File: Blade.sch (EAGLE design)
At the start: 100 parts, among them IC1 THN10-2411WIR, IC2 MCP6064-E/SL, IC3 MCP6064-E/SL, IC4 MCP6064-E/SL, Q1 12MHz, U1 ADR366WAUJZ, U2 ADR366WAUJZ, U3 ADS1148QPWRQ1, U4 ADS1148QPWRQ1, U5 ADS1148QPWRQ1, U6 LT1528, U7 S70FL01GS, U8 S70FL01GS, U9 STM32F77XXXLQFP208, X1 D-SUB9-H5M09RA, X2 D-SUB15-H5M15RA, X3 USBPTH

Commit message: opto added
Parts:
- added D5, D6, D7, D8, D9: 3V6, diodes:DZMELF
- added IC5: MAX488CSA, maxim:MAX488CSA
- added IC6, IC7: MOCD207MSOIC-8, Opto-Electronic:MOCD207MSOIC-8
- added R10: 1k, rcl:R-EU_R0805
- added RN11, RN12: 56k, resistor-dil:4R-NEXBS8V
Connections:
- new net EXP_IN: D5.C, IC5G$1.RO, U9.PE0
- new net EXP_OUT: D6.C, IC5G$1.DI, U9.PE1
- new net LO_OPT: D7.C, IC7.COL1, RN12C.2, U9.PI7
- new net N$42: IC6.A1, RN11C.2
- new net N$43: IC6.A2, RN11D.2
- new net N$45: IC7.COL2, RN12D.2
- new net N$46: IC7.A1, RN11A.2
- new net N$47: IC7.A2, RN11B.2
- new net N$48: IC7.C2
- new net SODS_OPT: D8.C, IC6.COL1, RN12A.2, U9.PI5
- new net SOE_OPT: D9.C, IC6.COL2, RN12B.2, U9.PI6
- net 28V: now also RN11A.1, RN11B.1, RN11C.1, RN11D.1
- net 3V3: now also IC5P.VCC, RN12A.1, RN12B.1, RN12C.1, RN12D.1
- net EXP_IN_N: now also IC5G$1.B, R10.1
- net EXP_IN_P: now also IC5G$1.A, R10.2
- net EXP_OUT_N: now also IC5G$1.Z
- net EXP_OUT_P: now also IC5G$1.Y
- net GND: now also D5.A, D6.A, D7.A, D8.A, D9.A, IC5P.GND, IC6.EMT1, IC6.EMT2, IC7.EMT1, IC7.EMT2
- net LO: now also IC7.C1
- net SODS: now also IC6.C1
- net SOE: now also IC6.C2

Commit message: cleanup
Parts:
- RN11: value 56k -> 3k
- RN12: value 56k -> 1k
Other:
- note added: "galv trenn?"
- moved on the sheet: C1, C10, C11, C12, C13, C14, C15, C19, C2, C20, C21, C22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

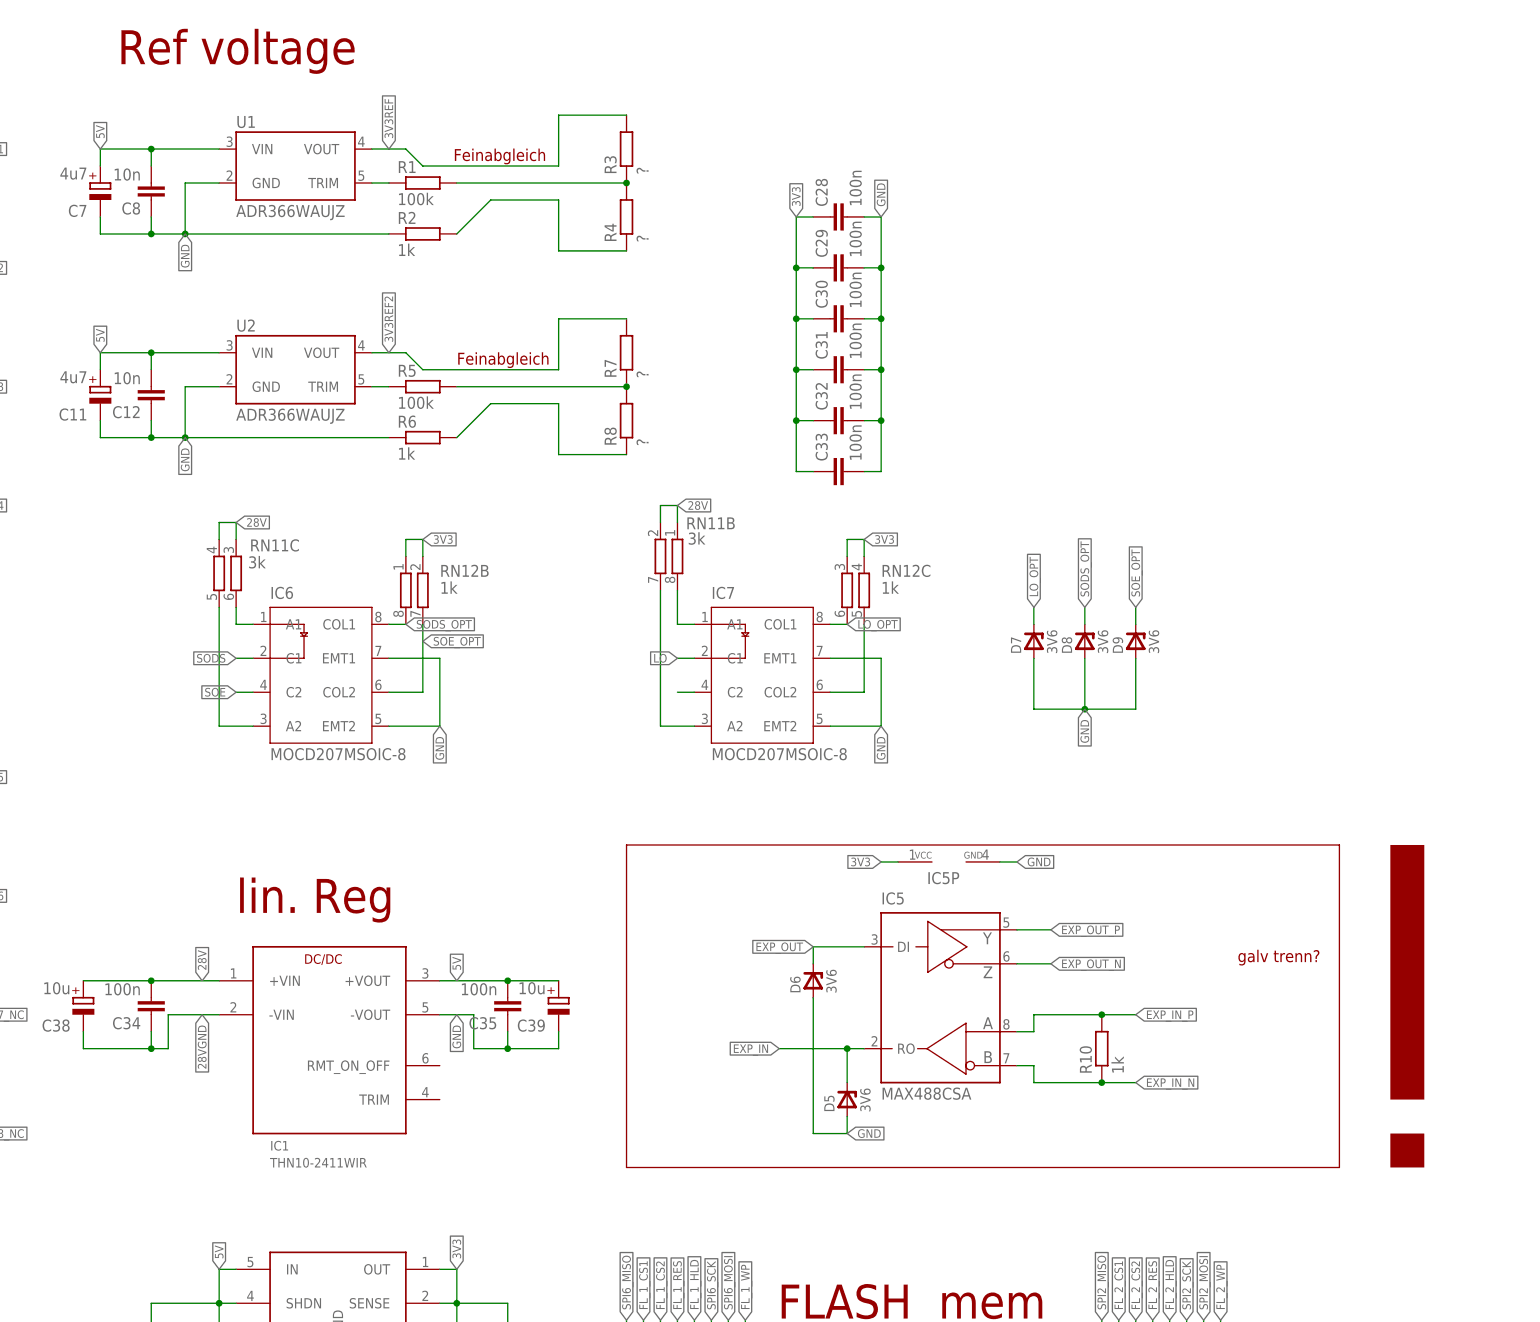
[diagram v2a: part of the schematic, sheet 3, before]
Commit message: RS422 opto galv isolation added
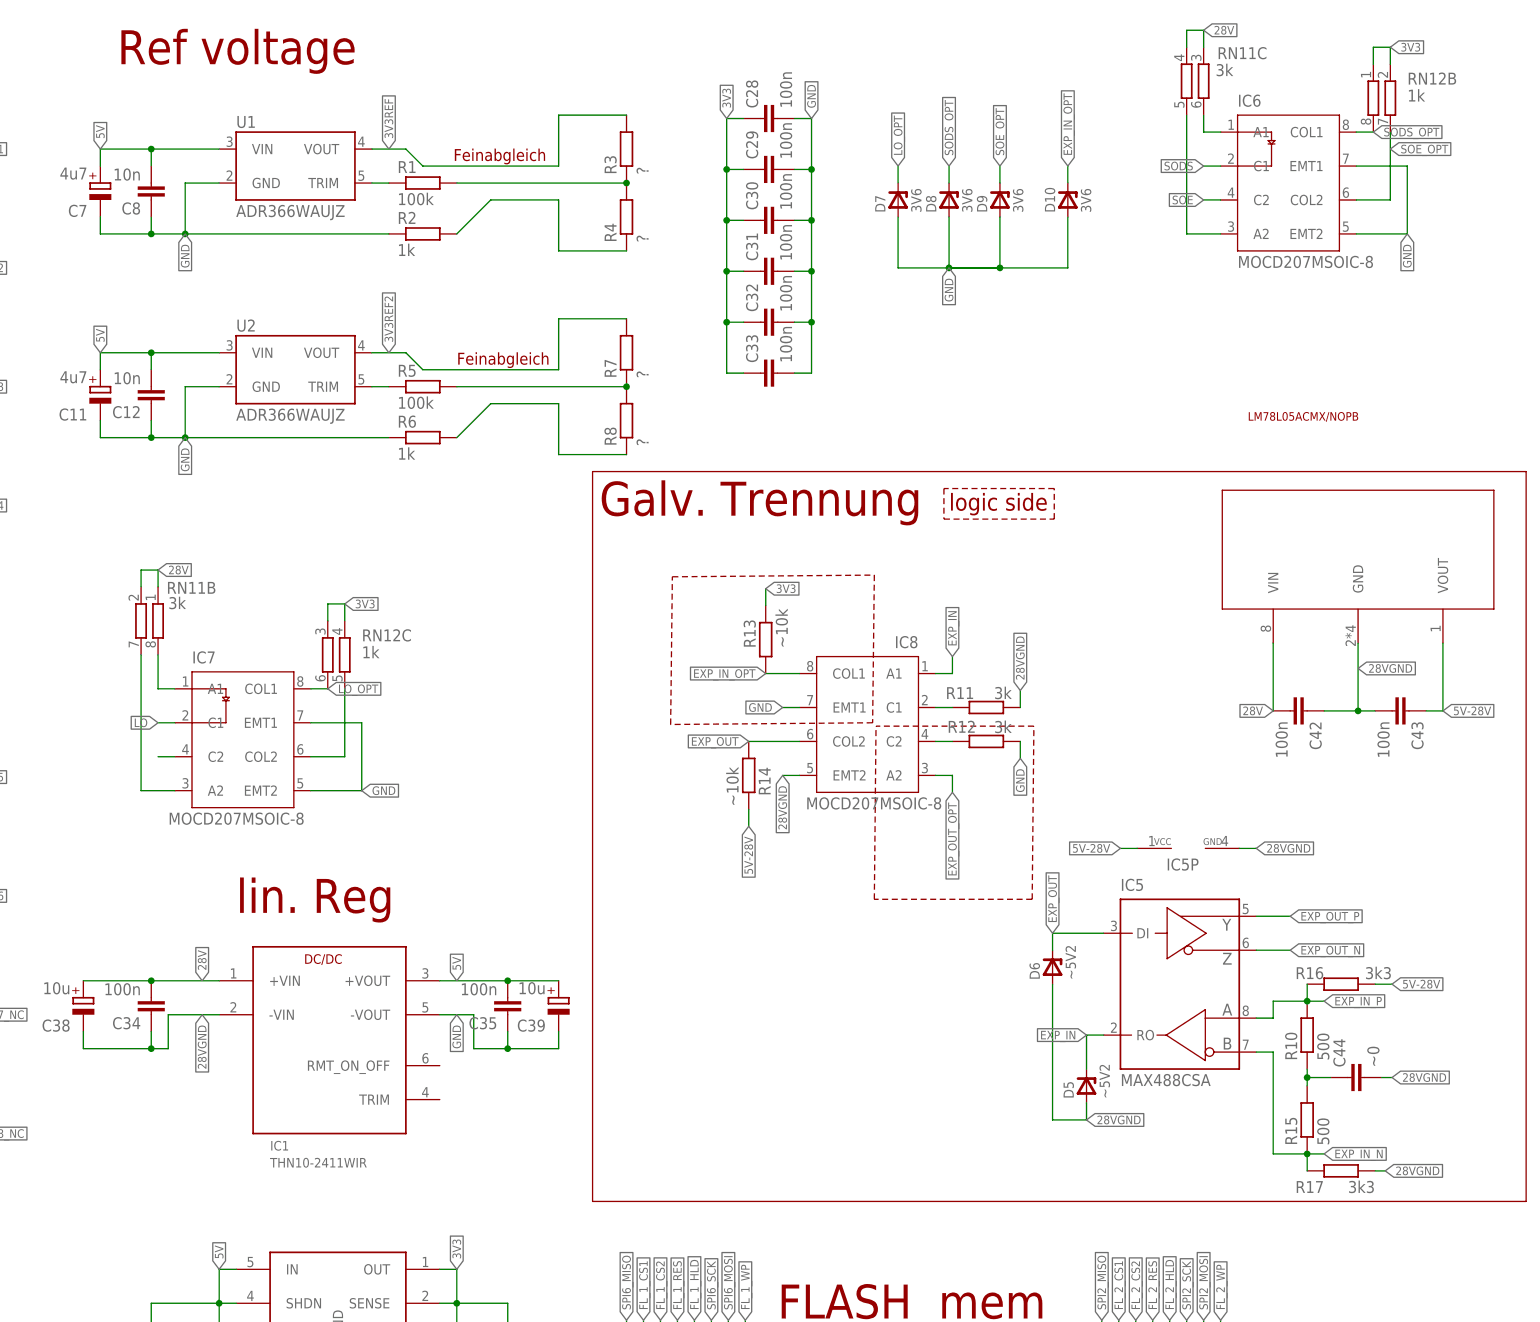
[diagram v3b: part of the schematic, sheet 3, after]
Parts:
- added C42, C43: 100n, rcl:C-EUC0805
- added C44: ~0, rcl:C-EUC0805
- added D10: 3V6, diodes:DZMELF
- added IC8: MOCD207MSOIC-8, Opto-Electronic:MOCD207MSOIC-8
- added R11, R12: 3k, rcl:R-EU_R0805
- added R13, R14: ~10k, rcl:R-EU_R0805
- added R15: 500, rcl:R-EU_R0805
- added R16, R17: 3k3, rcl:R-EU_R0805
- added U$1: LM78L05ACMX/NOPB, m-pad-2.1:LM78L05ACMX/NOPB
- D5, D6: value 3V6 -> ~5V2
- R10: value 1k -> 500
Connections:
- new net 5V-28V: C43.1, IC5P.VCC, R14.2, R16.1, U$1.VOUT
- new net EXP_IN_OPT: D10.C, IC8.COL1, R13.1
- new net EXP_OUT_OPT: IC8.A2
- new net N$44: IC8.C2, R12.2
- new net N$49: IC8.C1, R11.2
- new net N$50: C44.1, R10.1, R15.2
- net 28V: now also C42.2, U$1.VIN
- net 28VGND: now also C42.1, C43.2, C44.2, D5.A, D6.A, IC5P.GND, IC8.EMT2, R11.1, R17.1, U$1.GND
- net 3V3: now also R13.2; no longer IC5P.VCC
- net EXP_IN: now also IC8.A1
- net EXP_IN_N: now also R15.1, R17.2; no longer R10.1
- net EXP_IN_P: now also R16.2
- net EXP_OUT: now also IC8.COL2, R14.1
- net GND: now also D10.A, IC8.EMT1, R12.1; no longer D5.A, D6.A, IC5P.GND
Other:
- note added: "Galv. Trennung"
- note added: "LM78L05ACMX/NOPB"
- note added: "logic side"
- note removed: "galv trenn?"
- moved on the sheet: C28, C29, C30, C31, C32, C33, D5, D6, D7, D8, D9, IC5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

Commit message: rerouting
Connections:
- net 28V: no longer X1-8.F
- net 28VGND: now also X1-8.F
- net EXP_IN: no longer U9.PE0
- net EXP_IN_OPT: now also U9.PE0
- net EXP_OUT: no longer U9.PE1
- net EXP_OUT_OPT: now also U9.PE1
- net LED_1: now also U9.PF5
- net LED_2: now also U9.PF4
- net LED_3: now also U9.PF3
- net LED_4: now also U9.PI14
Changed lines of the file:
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@@
 </segment>
 </net>
-<net name="EXP_IN" class="0">
+<net name="EXP_OUT_OPT" class="0">
+<segment>
+<pinref part="U9" gate="G$1" pin="PE1"/>
+<wire x1="383.54" y1="142.24" x2="383.54" y2="137.16" width="0.1524" layer="91"/>
+<label x="383.54" y="137.16" size="1.27" layer="95" rot="R270" xref="yes"/>
+</segment>
+</net>
+<net name="EXP_IN_OPT" class="0">
 <segment>
 <pinref part="U9" gate="G$1" pin="PE0"/>
@@
 </segment>
 </net>
-<net name="EXP_OUT" class="0">
-<segment>
-<pinref part="U9" gate="G$1" pin="PE1"/>
-<wire x1="383.54" y1="142.24" x2="383.54" y2="137.16" width="0.1524" layer="91"/>
-<label x="383.54" y="137.16" size="1.27" layer="95" rot="R270" xref="yes"/>
+<net name="LED_1" class="0">
+<segment>
+<pinref part="U9" gate="G$1" pin="PF5"/>
+<wire x1="276.86" y1="142.24" x2="276.86" y2="137.16" width="0.1524" layer="91"/>
+<label x="276.86" y="137.16" size="1.27" layer="95" rot="R270" xref="yes"/>
+</segment>
+</net>
+<net name="LED_2" class="0">
+<segment>
+<pinref part="U9" gate="G$1" pin="PF4"/>
+<wire x1="281.94" y1="142.24" x2="281.94" y2="137.16" width="0.1524" layer="91"/>
+<label x="281.94" y="137.16" size="1.27" layer="95" rot="R270" xref="yes"/>
+</segment>
+</net>
+<net name="LED_3" class="0">
+<segment>
+<pinref part="U9" gate="G$1" pin="PF3"/>
+<wire x1="287.02" y1="142.24" x2="287.02" y2="137.16" width="0.1524" layer="91"/>
+<label x="287.02" y="137.16" size="1.27" layer="95" rot="R270" xref="yes"/>
+</segment>
+</net>
+<net name="LED_4" class="0">
+<segment>
+<pinref part="U9" gate="G$1" pin="PI14"/>
+<wire x1="210.82" y1="401.32" x2="205.74" y2="401.32" width="0.1524" layer="91"/>
+<label x="205.74" y="401.32" size="1.27" layer="95" rot="R180" xref="yes"/>
 </segment>
 </net>
@@
 </segment>
 <segment>
-<pinref part="X1" gate="-8" pin="F"/>
-<wire x1="104.14" y1="124.46" x2="109.22" y2="124.46" width="0.1524" layer="91"/>
-<wire x1="109.22" y1="124.46" x2="109.22" y2="127" width="0.1524" layer="91"/>
 <pinref part="X1" gate="-9" pin="F"/>
 <wire x1="109.22" y1="127" x2="104.14" y2="127" width="0.1524" layer="91"/>
@@
 <label x="106.68" y="172.72" size="1.27" layer="95" xref="yes"/>
 <pinref part="X2" gate="-15" pin="F"/>
+</segment>
+<segment>
+<pinref part="X1" gate="-8" pin="F"/>
+<wire x1="104.14" y1="124.46" x2="109.22" y2="124.46" width="0.1524" layer="91"/>
+<label x="109.22" y="124.46" size="1.27" layer="95" xref="yes"/>
 </segment>
 </net>
@@
 <wire x1="442.468" y1="226.06" x2="425.958" y2="226.06" width="0.1524" layer="94" style="shortdash"/>
 <wire x1="425.958" y1="226.06" x2="425.958" y2="221.488" width="0.1524" layer="94" style="shortdash"/>
+<wire x1="477.52" y1="256.54" x2="477.52" y2="297.18" width="0.1524" layer="94" style="shortdash"/>
+<wire x1="477.52" y1="297.18" x2="513.08" y2="297.18" width="0.1524" layer="94" style="shortdash"/>
+<wire x1="513.08" y1="297.18" x2="513.08" y2="256.54" width="0.1524" layer="94" style="shortdash"/>
+<wire x1="513.08" y1="256.54" x2="477.52" y2="256.54" width="0.1524" layer="94" style="shortdash"/>
 </plain>
 <instances>

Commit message: ground vias
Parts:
- added LED5, LED6, LED7, LED8: (no value), adafruit:LEDCHIP-LED0603
- added R18, R19, R20, R21: ?, rcl:R-EU_R0805
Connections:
- new net N$51: LED5.A, R18.1
- new net N$52: LED6.A, R19.1
- new net N$55: LED7.A, R20.1
- new net N$56: LED8.A, R21.1
- net 28V: now also R20.2
- net 28VGND: now also LED7.C, LED8.C
- net 3V3: now also R19.2
- net 5V: now also R18.2
- net 5V-28V: now also R21.2
- net GND: now also LED5.C, LED6.C
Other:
- note added: "V. Reg"
- note removed: "lin. Reg"
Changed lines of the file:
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@@
 <part name="R16" library="rcl" deviceset="R-EU_" device="R0805" value="3k3"/>
 <part name="R17" library="rcl" deviceset="R-EU_" device="R0805" value="3k3"/>
+<part name="LED5" library="adafruit" library_urn="urn:adsk.eagle:library:420" deviceset="LED" device="CHIP-LED0603" package3d_urn="urn:adsk.eagle:package:6240556/1"/>
+<part name="LED6" library="adafruit" library_urn="urn:adsk.eagle:library:420" deviceset="LED" device="CHIP-LED0603" package3d_urn="urn:adsk.eagle:package:6240556/1"/>
+<part name="R18" library="rcl" library_urn="urn:adsk.eagle:library:334" deviceset="R-EU_" device="R0805" package3d_urn="urn:adsk.eagle:package:23553/2" value="?"/>
+<part name="R19" library="rcl" library_urn="urn:adsk.eagle:library:334" deviceset="R-EU_" device="R0805" package3d_urn="urn:adsk.eagle:package:23553/2" value="?"/>
+<part name="LED7" library="adafruit" library_urn="urn:adsk.eagle:library:420" deviceset="LED" device="CHIP-LED0603" package3d_urn="urn:adsk.eagle:package:6240556/1"/>
+<part name="R20" library="rcl" library_urn="urn:adsk.eagle:library:334" deviceset="R-EU_" device="R0805" package3d_urn="urn:adsk.eagle:package:23553/2" value="?"/>
+<part name="LED8" library="adafruit" library_urn="urn:adsk.eagle:library:420" deviceset="LED" device="CHIP-LED0603" package3d_urn="urn:adsk.eagle:package:6240556/1"/>
+<part name="R21" library="rcl" library_urn="urn:adsk.eagle:library:334" deviceset="R-EU_" device="R0805" package3d_urn="urn:adsk.eagle:package:23553/2" value="?"/>
 </parts>
 <sheets>
@@
   UART</text>
 <text x="401.066" y="101.854" size="5.08" layer="94">FLASH  mem</text>
-<text x="320.04" y="162.56" size="5.08" layer="94">lin. Reg</text>
+<text x="320.04" y="162.56" size="5.08" layer="94">V. Reg</text>
 <wire x1="469.9" y1="279.4" x2="474.98" y2="279.4" width="0.1524" layer="94"/>
 <wire x1="474.98" y1="279.4" x2="474.98" y2="278.13" width="0.1524" layer="94"/>
@@
 <attribute name="NAME" x="25.4" y="73.152" size="1.778" layer="95"/>
 </instance>
+<instance part="LED5" gate="G$1" x="43.18" y="83.82" smashed="yes" rot="R90">
+<attribute name="NAME" x="47.752" y="87.376" size="1.778" layer="95" rot="R180"/>
+<attribute name="VALUE" x="47.752" y="89.535" size="1.778" layer="96" rot="R180"/>
+</instance>
+<instance part="LED6" gate="G$1" x="43.18" y="91.44" smashed="yes" rot="R90">
+<attribute name="NAME" x="47.752" y="94.996" size="1.778" layer="95" rot="R180"/>
+<attribute name="VALUE" x="47.752" y="97.155" size="1.778" layer="96" rot="R180"/>
+</instance>
+<instance part="R18" gate="G$1" x="33.02" y="83.82" smashed="yes" rot="R180">
+<attribute name="NAME" x="36.83" y="82.3214" size="1.778" layer="95" rot="R180"/>
+<attribute name="VALUE" x="36.83" y="87.122" size="1.778" layer="96" rot="R180"/>
+</instance>
+<instance part="R19" gate="G$1" x="33.02" y="91.44" smashed="yes" rot="R180">
+<attribute name="NAME" x="36.83" y="89.9414" size="1.778" layer="95" rot="R180"/>
+<attribute name="VALUE" x="36.83" y="94.742" size="1.778" layer="96" rot="R180"/>
+</instance>
+<instance part="LED7" gate="G$1" x="43.18" y="99.06" smashed="yes" rot="R90">
+<attribute name="NAME" x="47.752" y="102.616" size="1.778" layer="95" rot="R180"/>
+<attribute name="VALUE" x="47.752" y="104.775" size="1.778" layer="96" rot="R180"/>
+</instance>
+<instance part="R20" gate="G$1" x="33.02" y="99.06" smashed="yes" rot="R180">
+<attribute name="NAME" x="36.83" y="97.5614" size="1.778" layer="95" rot="R180"/>
+<attribute name="VALUE" x="36.83" y="102.362" size="1.778" layer="96" rot="R180"/>
+</instance>
+<instance part="LED8" gate="G$1" x="43.18" y="106.68" smashed="yes" rot="R90">
+<attribute name="NAME" x="47.752" y="110.236" size="1.778" layer="95" rot="R180"/>
+<attribute name="VALUE" x="47.752" y="112.395" size="1.778" layer="96" rot="R180"/>
+</instance>
+<instance part="R21" gate="G$1" x="33.02" y="106.68" smashed="yes" rot="R180">
+<attribute name="NAME" x="36.83" y="105.1814" size="1.778" layer="95" rot="R180"/>
+<attribute name="VALUE" x="36.83" y="109.982" size="1.778" layer="96" rot="R180"/>
+</instance>
 </instances>
 <busses>
@@
 <junction x="50.8" y="60.96"/>
 <label x="50.8" y="53.34" size="1.27" layer="95" xref="yes"/>
+<wire x1="50.8" y1="76.2" x2="50.8" y2="83.82" width="0.1524" layer="91"/>
+<junction x="50.8" y="76.2"/>
+<pinref part="LED6" gate="G$1" pin="C"/>
+<wire x1="50.8" y1="83.82" x2="50.8" y2="91.44" width="0.1524" layer="91"/>
+<wire x1="50.8" y1="91.44" x2="48.26" y2="91.44" width="0.1524" layer="91"/>
+<pinref part="LED5" gate="G$1" pin="C"/>
+<wire x1="48.26" y1="83.82" x2="50.8" y2="83.82" width="0.1524" layer="91"/>
+<junction x="50.8" y="83.82"/>
 </segment>
 </net>
@@
 </segment>
 </net>
+<net name="N$51" class="0">
+<segment>
+<pinref part="LED5" gate="G$1" pin="A"/>
+<pinref part="R18" gate="G$1" pin="1"/>
+<wire x1="38.1" y1="83.82" x2="40.64" y2="83.82" width="0.1524" layer="91"/>
+</segment>
+</net>
+<net name="N$52" class="0">
+<segment>
+<pinref part="LED6" gate="G$1" pin="A"/>
+<pinref part="R19" gate="G$1" pin="1"/>
+<wire x1="38.1" y1="91.44" x2="40.64" y2="91.44" width="0.1524" layer="91"/>
+</segment>
+</net>
+<net name="5V" class="0">
+<segment>
+<pinref part="R18" gate="G$1" pin="2"/>
+<wire x1="27.94" y1="83.82" x2="25.4" y2="83.82" width="0.1524" layer="91"/>
+<label x="25.4" y="83.82" size="1.27" layer="95" rot="R180" xref="yes"/>
+</segment>
+</net>
+<net name="3V3" class="0">
+<segment>
+<pinref part="R19" gate="G$1" pin="2"/>
+<wire x1="27.94" y1="91.44" x2="25.4" y2="91.44" width="0.1524" layer="91"/>
+<label x="25.4" y="91.44" size="1.27" layer="95" rot="R180" xref="yes"/>
+</segment>
+</net>
+<net name="28VGND" class="0">
+<segment>
+<pinref part="LED7" gate="G$1" pin="C"/>
+<wire x1="48.26" y1="99.06" x2="50.8" y2="99.06" width="0.1524" layer="91"/>
+<wire x1="50.8" y1="99.06" x2="50.8" y2="106.68" width="0.1524" layer="91"/>
+<pinref part="LED8" gate="G$1" pin="C"/>
+<wire x1="50.8" y1="106.68" x2="48.26" y2="106.68" width="0.1524" layer="91"/>
+<label x="50.8" y="106.68" size="1.27" layer="95" xref="yes"/>
+</segment>
+</net>
+<net name="28V" class="0">
+<segment>
+<pinref part="R20" gate="G$1" pin="2"/>
+<wire x1="27.94" y1="99.06" x2="25.4" y2="99.06" width="0.1524" layer="91"/>
+<label x="25.4" y="99.06" size="1.27" layer="95" rot="R180" xref="yes"/>
+</segment>
+</net>
+<net name="N$55" class="0">
+<segment>
+<pinref part="R20" gate="G$1" pin="1"/>
+<pinref part="LED7" gate="G$1" pin="A"/>
+<wire x1="38.1" y1="99.06" x2="40.64" y2="99.06" width="0.1524" layer="91"/>
+</segment>
+</net>
+<net name="N$56" class="0">
+<segment>
+<pinref part="LED8" gate="G$1" pin="A"/>
+<pinref part="R21" gate="G$1" pin="1"/>
+<wire x1="40.64" y1="106.68" x2="38.1" y2="106.68" width="0.1524" layer="91"/>
+</segment>
+</net>
+<net name="5V-28V" class="0">
+<segment>
+<pinref part="R21" gate="G$1" pin="2"/>
+<wire x1="27.94" y1="106.68" x2="25.4" y2="106.68" width="0.1524" layer="91"/>
+<label x="25.4" y="106.68" size="1.27" layer="95" rot="R180" xref="yes"/>
+</segment>
+</net>
